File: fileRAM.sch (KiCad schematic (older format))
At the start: 13 parts, among them J3 MM1_5530843-2, U34 74LVC1G34, U35 74AHC273, U36 74AHC1G04, U37 74AHC273, U38 74AHC374, U39 74AHC1G04

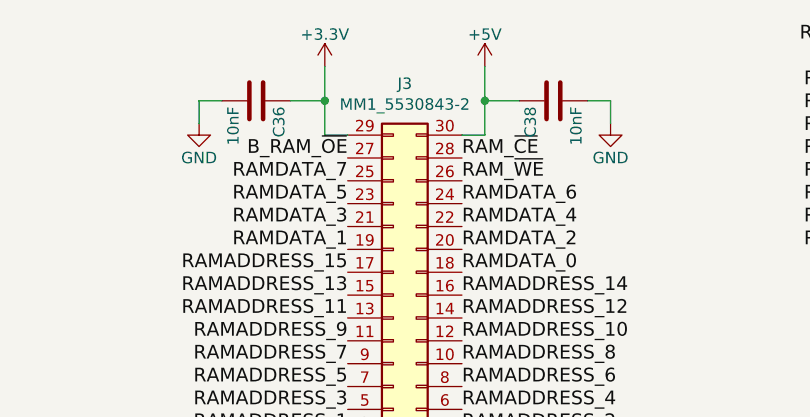
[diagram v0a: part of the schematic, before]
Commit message: Better decoupling #6
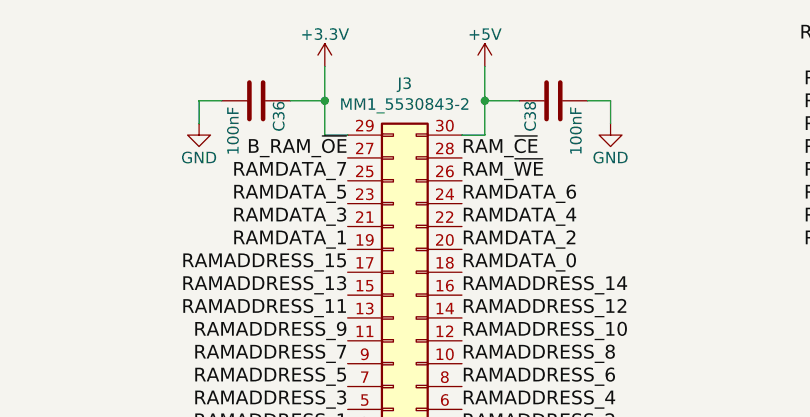
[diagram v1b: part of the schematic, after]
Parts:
- C36, C38: value 10nF -> 100nF
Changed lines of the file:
@@
 U 1 1 5B0E7716
 P 7150 1100
-F 0 "C36" H 7175 1200 50  0000 L CNN
-F 1 "10nF" H 7175 1000 50  0000 L CNN
+F 0 "C36" H 7150 1200 50  0000 L CNN
+F 1 "100nF" H 7175 1000 50  0000 L CNN
 F 2 "Capacitor_SMD:C_0805_2012Metric" H 7188 950 50  0001 C CNN
 F 3 "" H 7150 1100 50  0001 C CNN
@@
 U 1 1 5B0E7789
 P 8450 1100
-F 0 "C38" H 8475 1200 50  0000 L CNN
-F 1 "10nF" H 8475 1000 50  0000 L CNN
+F 0 "C38" H 8450 1200 50  0000 L CNN
+F 1 "100nF" H 8475 1000 50  0000 L CNN
 F 2 "Capacitor_SMD:C_0805_2012Metric" H 8488 950 50  0001 C CNN
 F 3 "" H 8450 1100 50  0001 C CNN
